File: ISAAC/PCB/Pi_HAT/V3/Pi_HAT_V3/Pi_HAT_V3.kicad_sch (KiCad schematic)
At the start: 8 parts, among them J1 MPU 6050, J2 Pi_GPIO, J3 Display, J7 Pressure Sensor

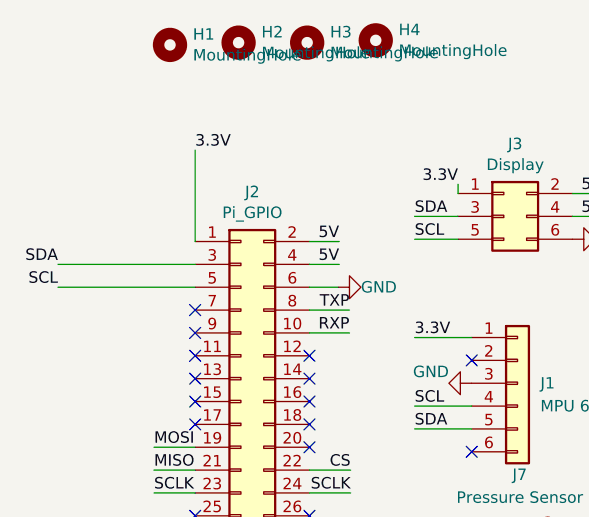
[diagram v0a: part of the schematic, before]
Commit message: Updated Moteus PCB
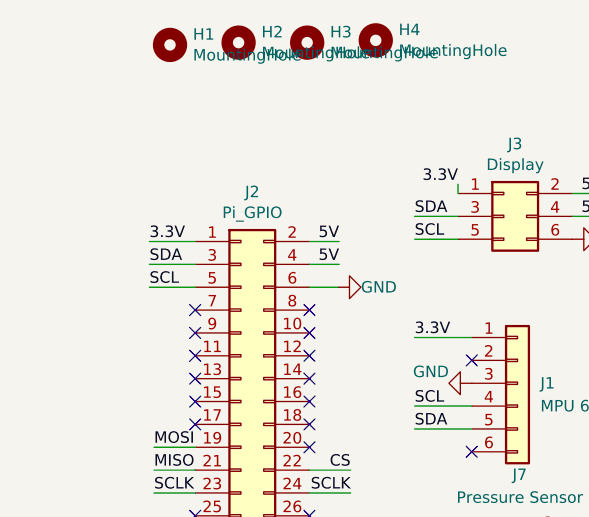
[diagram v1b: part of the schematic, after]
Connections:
- net RXP: no longer names the net of J2.10 (Pin_10)
- net TXP: no longer names the net of J2.8 (Pin_8)
- no-connect marks 29 -> 31
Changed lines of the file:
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@@
   (no_connect (at 112.776 98.044))
   (no_connect (at 143.51 75.692))
+  (no_connect (at 125.476 70.104))
+  (no_connect (at 125.476 72.644))
   (no_connect (at 125.476 92.964))
   (no_connect (at 125.476 100.584))
@@
     (stroke (width 0) (type default) (color 0 0 0 0))
   )
-  (wire (pts (xy 97.536 65.024) (xy 112.776 65.024))
-    (stroke (width 0) (type default) (color 0 0 0 0))
-  )
-  (wire (pts (xy 112.776 52.324) (xy 112.776 62.484))
+  (wire (pts (xy 107.696 62.484) (xy 112.776 62.484))
     (stroke (width 0) (type default) (color 0 0 0 0))
   )
@@
   )
   (wire (pts (xy 182.626 123.19) (xy 187.198 123.19))
+    (stroke (width 0) (type default) (color 0 0 0 0))
+  )
+  (wire (pts (xy 107.696 67.564) (xy 112.776 67.564))
     (stroke (width 0) (type default) (color 0 0 0 0))
   )
@@
     (stroke (width 0) (type default) (color 0 0 0 0))
   )
-  (wire (pts (xy 129.921 70.104) (xy 125.476 70.104))
-    (stroke (width 0) (type default) (color 0 0 0 0))
-  )
   (wire (pts (xy 183.642 78.486) (xy 187.452 78.486))
     (stroke (width 0) (type default) (color 0 0 0 0))
   )
   (wire (pts (xy 182.626 125.476) (xy 187.198 125.476))
+    (stroke (width 0) (type default) (color 0 0 0 0))
+  )
+  (wire (pts (xy 107.696 65.024) (xy 112.776 65.024))
     (stroke (width 0) (type default) (color 0 0 0 0))
   )
@@
     (stroke (width 0) (type default) (color 0 0 0 0))
   )
-  (wire (pts (xy 97.536 67.564) (xy 112.776 67.564))
-    (stroke (width 0) (type default) (color 0 0 0 0))
-  )
   (wire (pts (xy 141.986 62.23) (xy 137.16 62.23))
     (stroke (width 0) (type default) (color 0 0 0 0))
@@
   )
   (wire (pts (xy 108.204 85.344) (xy 112.776 85.344))
-    (stroke (width 0) (type default) (color 0 0 0 0))
-  )
-  (wire (pts (xy 129.921 72.644) (xy 125.476 72.644))
     (stroke (width 0) (type default) (color 0 0 0 0))
   )
@@
     (effects (font (size 1.27 1.27)) (justify right bottom))
   )
-  (label "TXP" (at 129.921 70.104 180)
-    (effects (font (size 1.27 1.27)) (justify right bottom))
-  )
-  (label "SDA" (at 97.536 65.024 180)
-    (effects (font (size 1.27 1.27)) (justify right bottom))
+  (label "SDA" (at 107.696 65.024 0)
+    (effects (font (size 1.27 1.27)) (justify left bottom))
   )
   (label "SCL" (at 137.16 62.23 0)
@@
     (effects (font (size 1.27 1.27)) (justify left bottom))
   )
-  (label "3.3V" (at 112.776 52.324 0)
+  (label "3.3V" (at 107.696 62.484 0)
     (effects (font (size 1.27 1.27)) (justify left bottom))
   )
@@
     (effects (font (size 1.27 1.27)) (justify left bottom))
   )
-  (label "SCL" (at 97.536 67.564 180)
-    (effects (font (size 1.27 1.27)) (justify right bottom))
+  (label "SCL" (at 107.696 67.564 0)
+    (effects (font (size 1.27 1.27)) (justify left bottom))
   )
   (label "SDA" (at 137.16 59.69 0)
@@
     (effects (font (size 1.27 1.27)) (justify right bottom))
   )
-  (label "RXP" (at 129.921 72.644 180)
-    (effects (font (size 1.27 1.27)) (justify right bottom))
-  )

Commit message: Shit ton of stuf
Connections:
- net CS: now also J2.24 (Pin_24); no longer J2.22 (Pin_22)
- net SCLK: no longer J2.24 (Pin_24)
- no-connect marks 31 -> 32
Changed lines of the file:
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@@
   (no_connect (at 125.476 77.724))
   (no_connect (at 125.476 75.184))
+  (no_connect (at 125.476 87.884))
   (no_connect (at 112.776 98.044))
   (no_connect (at 143.51 75.692))
@@
     (stroke (width 0) (type default) (color 0 0 0 0))
   )
-  (wire (pts (xy 130.048 90.424) (xy 125.476 90.424))
-    (stroke (width 0) (type default) (color 0 0 0 0))
-  )
   (wire (pts (xy 137.16 83.312) (xy 143.51 83.312))
     (stroke (width 0) (type default) (color 0 0 0 0))
@@
     (stroke (width 0) (type default) (color 0 0 0 0))
   )
-  (wire (pts (xy 125.476 87.884) (xy 130.048 87.884))
+  (wire (pts (xy 125.476 90.424) (xy 130.048 90.424))
     (stroke (width 0) (type default) (color 0 0 0 0))
   )
@@
     (effects (font (size 1.27 1.27)) (justify right bottom))
   )
-  (label "CS" (at 130.048 87.884 180)
+  (label "CS" (at 130.048 90.424 180)
     (effects (font (size 1.27 1.27)) (justify right bottom))
   )
@@
   (label "SCLK" (at 182.626 127.762 0)
     (effects (font (size 1.27 1.27)) (justify left bottom))
-  )
-  (label "SCLK" (at 130.048 90.424 180)
-    (effects (font (size 1.27 1.27)) (justify right bottom))
   )
   (label "5V" (at 128.778 62.484 180)
@@
       (reference "J8") (unit 1) (value "XT60PW-M") (footprint ".pretty:AMASS_XT60PW-M")
     )
+    (path "/048aae1f-d538-461c-a17b-6a2498319945/01285383-513e-4f70-b632-92801497d57d"
+      (reference "J9") (unit 1) (value "JST-BATT") (footprint "Connector_PinHeader_2.54mm:PinHeader_1x04_P2.54mm_Vertical")
+    )
     (path "/00000000-0000-0000-0000-00006251fa46/f8261744-a8f9-42f6-8adc-0b665396d639"

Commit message: Final Updates "HOPEFULLY"
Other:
- sheet A-D Converter ports: added VCC0, VCC1; removed none
- sheet Buck Converter ports: added VCC0, VCC1; removed none
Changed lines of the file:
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@@
+    (stroke (width 0) (type default) (color 0 0 0 0))
+  )
+  (wire (pts (xy 183.388 67.31) (xy 187.452 67.31))
+    (stroke (width 0) (type default) (color 0 0 0 0))
+  )
+  (wire (pts (xy 182.372 89.408) (xy 187.452 89.408))
     (stroke (width 0) (type default) (color 0 0 0 0))
   )
@@
     (stroke (width 0) (type default) (color 0 0 0 0))
   )
-  (wire (pts (xy 183.642 78.486) (xy 187.452 78.486))
+  (wire (pts (xy 182.118 134.62) (xy 187.198 134.62))
+    (stroke (width 0) (type default) (color 0 0 0 0))
+  )
+  (wire (pts (xy 183.388 78.486) (xy 187.452 78.486))
     (stroke (width 0) (type default) (color 0 0 0 0))
   )
@@
     (stroke (width 0) (type default) (color 0 0 0 0))
   )
-  (wire (pts (xy 187.452 67.31) (xy 184.15 67.31))
-    (stroke (width 0) (type default) (color 0 0 0 0))
-  )
   (wire (pts (xy 141.986 62.23) (xy 137.16 62.23))
     (stroke (width 0) (type default) (color 0 0 0 0))
   )
-  (wire (pts (xy 187.452 72.898) (xy 183.642 72.898))
+  (wire (pts (xy 183.388 72.898) (xy 187.452 72.898))
     (stroke (width 0) (type default) (color 0 0 0 0))
   )
@@
     (stroke (width 0) (type default) (color 0 0 0 0))
   )
+  (wire (pts (xy 182.372 84.328) (xy 187.452 84.328))
+    (stroke (width 0) (type default) (color 0 0 0 0))
+  )
   (wire (pts (xy 108.204 85.344) (xy 112.776 85.344))
     (stroke (width 0) (type default) (color 0 0 0 0))
@@
     (stroke (width 0) (type default) (color 0 0 0 0))
   )
+  (wire (pts (xy 182.118 137.16) (xy 187.198 137.16))
+    (stroke (width 0) (type default) (color 0 0 0 0))
+  )
   (label "5V" (at 128.778 65.024 180)
     (effects (font (size 1.27 1.27)) (justify right bottom))
@@
     (effects (font (size 1.27 1.27)) (justify right bottom))
   )
+  (label "12V1" (at 182.372 89.408 0)
+    (effects (font (size 1.27 1.27)) (justify left bottom))
+  )
   (label "SDA" (at 107.696 65.024 0)
     (effects (font (size 1.27 1.27)) (justify left bottom))
@@
     (effects (font (size 1.27 1.27)) (justify left bottom))
   )
-  (label "SDA" (at 183.642 72.898 0)
+  (label "SDA" (at 183.388 72.898 0)
     (effects (font (size 1.27 1.27)) (justify left bottom))
   )
@@
     (effects (font (size 1.27 1.27)) (justify left bottom))
   )
+  (label "12V0" (at 182.118 134.62 0)
+    (effects (font (size 1.27 1.27)) (justify left bottom))
+  )
   (label "CS" (at 182.626 130.048 0)
     (effects (font (size 1.27 1.27)) (justify left bottom))
@@
     (effects (font (size 1.27 1.27)) (justify right bottom))
   )
+  (label "12V1" (at 182.118 137.16 0)
+    (effects (font (size 1.27 1.27)) (justify left bottom))
+  )
   (label "MISO" (at 182.626 123.19 0)
     (effects (font (size 1.27 1.27)) (justify left bottom))
@@
     (effects (font (size 1.27 1.27)) (justify left bottom))
   )
-  (label "5V" (at 184.15 67.31 0)
+  (label "5V" (at 183.388 67.31 0)
     (effects (font (size 1.27 1.27)) (justify left bottom))
   )
@@
     (effects (font (size 1.27 1.27)) (justify left bottom))
   )
-  (label "SCL" (at 183.642 78.486 0)
+  (label "SCL" (at 183.388 78.486 0)
     (effects (font (size 1.27 1.27)) (justify left bottom))
   )
@@
   )
   (label "SCLK" (at 182.626 127.762 0)
+    (effects (font (size 1.27 1.27)) (justify left bottom))
+  )
+  (label "12V0" (at 182.372 84.328 0)
     (effects (font (size 1.27 1.27)) (justify left bottom))
   )
@@
     )
   )
-  (symbol (lib_id "Mechanical:MountingHole") (at 132.842 40.132 0) (unit 1)
-    (in_bom yes) (on_board yes)
-    (property "Reference" "H4" (id 0) (at 135.382 38.9636 0)
-      (effects (font (size 1.27 1.27)) (justify left))
-    )
-    (property "Value" "MountingHole" (id 1) (at 135.382 41.275 0)
-      (effects (font (size 1.27 1.27)) (justify left))
-    )
-    (property "Footprint" "MountingHole:MountingHole_2.5mm" (id 2) (at 132.842 40.132 0)
-      (effects (font (size 1.27 1.27)) hide)
-    )
-    (property "Datasheet" "~" (id 3) (at 132.842 40.132 0)
+  (symbol (lib_id "Mechanical:MountingHole") (at 132.842 40.386 0) (unit 1)
+    (in_bom yes) (on_board yes)
+    (property "Reference" "H4" (id 0) (at 135.382 39.2176 0)
+      (effects (font (size 1.27 1.27)) (justify left))
+    )
+    (property "Value" "MountingHole" (id 1) (at 135.382 41.529 0)
+      (effects (font (size 1.27 1.27)) (justify left))
+    )
+    (property "Footprint" "MountingHole:MountingHole_2.5mm" (id 2) (at 132.842 40.386 0)
+      (effects (font (size 1.27 1.27)) hide)
+    )
+    (property "Datasheet" "~" (id 3) (at 132.842 40.386 0)
       (effects (font (size 1.27 1.27)) hide)
     )
@@
       (effects (font (size 1.27 1.27)) (justify left))
     )
+    (pin "VCC0" input (at 187.452 84.328 180)
+      (effects (font (size 1.27 1.27)) (justify left))
+    )
+    (pin "VCC1" input (at 187.452 89.408 180)
+      (effects (font (size 1.27 1.27)) (justify left))
+    )
   )
   (sheet (at 187.198 116.332) (size 68.834 31.242) (fields_autoplaced)
@@
       (effects (font (size 1.27 1.27)) (justify left))
     )
+    (pin "VCC0" input (at 187.198 134.62 180)
+      (effects (font (size 1.27 1.27)) (justify left))
+    )
+    (pin "VCC1" input (at 187.198 137.16 180)
+      (effects (font (size 1.27 1.27)) (justify left))
+    )
   )
   (sheet_instances
@@
   )
   (symbol_instances
-    (path "/00000000-0000-0000-0000-00006251fa46/3eccf421-a11d-4ff1-b12e-7c823a1586c9"
+    (path "/00000000-0000-0000-0000-00006251fa46/34919398-a320-4878-bc46-06cd95143131"
       (reference "#FLG0101") (unit 1) (value "PWR_FLAG") (footprint "")
     )
@@
       (reference "#PWR0104") (unit 1) (value "GND") (footprint "")
     )
-    (path "/00000000-0000-0000-0000-00006251fa46/782f9291-1539-4a61-909e-da764fbb999c"
-      (reference "#PWR0105") (unit 1) (value "~") (footprint "")
+    (path "/048aae1f-d538-461c-a17b-6a2498319945/fb4b9f0c-ce5d-4c8a-b2dd-b3c62ec76aad"
+      (reference "#PWR0105") (unit 1) (value "GND") (footprint "")
     )
     (path "/00000000-0000-0000-0000-00006251fa46/00000000-0000-0000-0000-0000625334fb"
@@
       (reference "#PWR0109") (unit 1) (value "GND") (footprint "")
     )
-    (path "/00000000-0000-0000-0000-00006251fa46/087212ef-db18-4170-99e1-38075c9c4160"
-      (reference "#PWR0110") (unit 1) (value "~") (footprint "")
+    (path "/048aae1f-d538-461c-a17b-6a2498319945/37b893c9-a690-46f8-95d3-50f4d6ad15e5"
+      (reference "#PWR0110") (unit 1) (value "GND") (footprint "")
     )
     (path "/a123b3ab-3b36-4d53-924e-c900d59e4009"
@@
       (reference "J8") (unit 1) (value "XT60PW-M") (footprint ".pretty:AMASS_XT60PW-M")
     )
-    (path "/048aae1f-d538-461c-a17b-6a2498319945/01285383-513e-4f70-b632-92801497d57d"
-      (reference "J9") (unit 1) (value "JST-BATT") (footprint "Connector_PinHeader_2.54mm:PinHeader_1x04_P2.54mm_Vertical")
-    )
     (path "/00000000-0000-0000-0000-00006251fa46/f8261744-a8f9-42f6-8adc-0b665396d639"
       (reference "L1") (unit 1) (value "4.9u") (footprint ".pretty:744777004")
@@
       (reference "L2") (unit 1) (value "220u") (footprint ".pretty:IND_AIRD-02-151K")
     )
+    (path "/048aae1f-d538-461c-a17b-6a2498319945/6d115c07-f9e3-4e27-950f-6fdfcebadf48"
+      (reference "R1") (unit 1) (value "2k") (footprint "Resistor_SMD:R_0805_2012Metric_Pad1.20x1.40mm_HandSolder")
+    )
     (path "/00000000-0000-0000-0000-00006251fa46/3958159c-4a64-4fe6-ad0f-23afd9a4b82b"
       (reference "R2") (unit 1) (value "604k") (footprint "Resistor_SMD:R_1206_3216Metric_Pad1.30x1.75mm_HandSolder")
@@
       (reference "R5") (unit 1) (value "7.68K") (footprint "Resistor_SMD:R_0805_2012Metric_Pad1.20x1.40mm_HandSolder")
     )
+    (path "/048aae1f-d538-461c-a17b-6a2498319945/43135a2b-47e4-4e8e-ba56-03f3a7fec4fa"
+      (reference "R6") (unit 1) (value "1k") (footprint "Resistor_SMD:R_0805_2012Metric_Pad1.20x1.40mm_HandSolder")
+    )
+    (path "/048aae1f-d538-461c-a17b-6a2498319945/c16225f9-0eec-4fbe-9f60-7a7eeb058643"
+      (reference "R7") (unit 1) (value "2k") (footprint "Resistor_SMD:R_0805_2012Metric_Pad1.20x1.40mm_HandSolder")
+    )
+    (path "/048aae1f-d538-461c-a17b-6a2498319945/0898f807-8aba-4ca4-9c5f-fd6aa29c94e5"
+      (reference "R8") (unit 1) (value "1k") (footprint "Resistor_SMD:R_0805_2012Metric_Pad1.20x1.40mm_HandSolder")
+    )
     (path "/00000000-0000-0000-0000-00006251fa46/0babeadc-b38f-478d-a52d-d91f4677b2e1"
